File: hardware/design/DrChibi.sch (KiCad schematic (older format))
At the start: 20 parts, among them P1 PAD_SMD, P3 MultiPort, P4 IN+, P5 IN-, X1 MINI-USB-SHIELD-32005-201

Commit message: Six-phase power stage.
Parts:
- Rled3: renamed from R22; value 2k2 -> 100
- renumbered D2 to D1, D1 to D2, D4 to Dusb1, P3 to P1, P1 to P2, P4 to P3, P5 to P4, R14 to R1, R15 to R2, R38 to Rled1, R37 to Rled2, R6 to Rusb1, R103 to Rusb2, R104 to Rusb3
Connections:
- wire segments 74 -> 135
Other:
- moved on the sheet: Cbattfilt1, D1, D2, D3, Dusb1, P2, P3, P4, R1, R2, Rbatth1, Rbattl1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

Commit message: TODO: Routing of the DSBL-signals.
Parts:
- renumbered P1 to CONN1
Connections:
- wire segments 135 -> 142
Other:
- moved on the sheet: P3, P4
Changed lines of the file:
@@
 $Descr A4 11693 8268
 encoding utf-8
-Sheet 1 12
+Sheet 1 11
 Title "Long-Strip"
 Date "2016-02-15"
@@
 L CONN_1 P4
 U 1 1 53FA5B63
-P 9250 1350
-F 0 "P4" H 9330 1350 40  0000 L CNN
-F 1 "IN-" H 9250 1405 30  0001 C CNN
-F 2 "CRF1:1PAD_4x5mm" H 9250 1350 60  0001 C CNN
-F 3 "" H 9250 1350 60  0001 C CNN
-	1    9250 1350
+P 9250 2750
+F 0 "P4" H 9330 2750 40  0000 L CNN
+F 1 "IN-" H 9250 2805 30  0001 C CNN
+F 2 "CRF1:1PAD_4x5mm" H 9250 2750 60  0001 C CNN
+F 3 "" H 9250 2750 60  0001 C CNN
+	1    9250 2750
 	-1   0    0    1
 $EndComp
@@
 L CONN_1 P3
 U 1 1 53FA5B6A
-P 9250 1150
-F 0 "P3" H 9330 1150 40  0000 L CNN
-F 1 "IN+" H 9250 1205 30  0001 C CNN
-F 2 "CRF1:1PAD_4x5mm" H 9250 1150 60  0001 C CNN
-F 3 "" H 9250 1150 60  0001 C CNN
-	1    9250 1150
+P 9250 2550
+F 0 "P3" H 9330 2550 40  0000 L CNN
+F 1 "IN+" H 9250 2605 30  0001 C CNN
+F 2 "CRF1:1PAD_4x5mm" H 9250 2550 60  0001 C CNN
+F 3 "" H 9250 2550 60  0001 C CNN
+	1    9250 2550
 	-1   0    0    1
 $EndComp
@@
 DrChibi
 $Bitmap
-Pos 10700 3200
+Pos 10800 5000
 Scale 1,000000
 Data
@@
 	0    1    1    0
 $EndComp
-Text Notes 10050 1500 0    40   ~ 0
+Text Notes 10050 2900 0    40   ~ 0
 Voltage supply (5 - 24V)\nNeeds external decoupling\ncaps to avoid high voltage\ntransients produced by the\ninductance of the battery\nwiring while switching the FETs\nAlso critical for EMI/RF compliance
 $Comp
@@
 $EndSheet
 $Bitmap
-Pos 9700 5500
+Pos 9650 6250
 Scale 0,000000
 Data
@@
 EndData
 $EndBitmap
-Text Notes 9150 4900 0    60   ~ 0
+Text Notes 9100 5650 0    60   ~ 0
 Connect signal ground and\npower ground in one place only
 $Sheet
@@
 $EndComp
 $Sheet
-S 9650 2250 900  500
+S 9450 3350 900  500
 U 504F83BE
 F0 "Power Supply" 60
@@
 Connection ~ 2250 1100
 Wire Wire Line
-	9400 1450 9400 1350
-Wire Wire Line
-	10050 2700 10050 2700
+	9400 2850 9400 2750
 Wire Wire Line
 	2050 1900 1350 1900
@@
 	2550 2000 3150 2000
 Wire Notes Line
-	8950 900  10000 900
+	8950 2300 10000 2300
 Wire Notes Line
-	10000 950  10000 1650
+	10000 2350 10000 3050
 Wire Notes Line
-	10000 1650 8950 1650
+	10000 3050 8950 3050
 Wire Wire Line
 	2250 6000 2250 6000
@@
 	3150 2800 2750 2800
 $Sheet
-S 7550 750  800  400
+S 7900 750  800  900
 U 55DFCB16
 F0 "Virtual Y" 60
 F1 "virtual_y.sch" 60
-F2 "SENS1" I L 7550 800 60
-F3 "SENS2" I L 7550 900 60
-F4 "SENS3" I L 7550 1000 60
-F5 "SENSY" O L 7550 1100 60
+F2 "SENS1" I L 7900 800 60
+F3 "SENS2" I L 7900 900 60
+F4 "SENS3" I L 7900 1000 60
+F5 "SENSY1" O L 7900 1100 60
+F6 "SENS4" I L 7900 1250 60
+F7 "SENS5" I L 7900 1350 60
+F8 "SENS6" I L 7900 1450 60
+F9 "SENSY2" O L 7900 1600 60
 $EndSheet
 $Comp
-L GND #PWR11
+L GND #PWR01
 U 1 1 55E3ABA6
-P 9500 5150
-F 0 "#PWR11" H 9500 4900 50  0001 C CNN
-F 1 "GND" H 9500 5000 50  0000 C CNN
-F 2 "" H 9500 5150 60  0000 C CNN
-F 3 "" H 9500 5150 60  0000 C CNN
-	1    9500 5150
+P 9450 5900
+F 0 "#PWR01" H 9450 5650 50  0001 C CNN
+F 1 "GND" H 9450 5750 50  0000 C CNN
+F 2 "" H 9450 5900 60  0000 C CNN
+F 3 "" H 9450 5900 60  0000 C CNN
+	1    9450 5900
 	1    0    0    -1
 $EndComp
 $Comp
-L GNDPWR #PWR12
+L GNDPWR #PWR02
 U 1 1 55E3ADE6
-P 9800 5150
-F 0 "#PWR12" H 9800 4950 50  0001 C CNN
-F 1 "GNDPWR" H 9800 5020 50  0000 C CNN
-F 2 "" H 9800 5100 60  0000 C CNN
-F 3 "" H 9800 5100 60  0000 C CNN
-	1    9800 5150
+P 9750 5900
+F 0 "#PWR02" H 9750 5700 50  0001 C CNN
+F 1 "GNDPWR" H 9750 5770 50  0000 C CNN
+F 2 "" H 9750 5850 60  0000 C CNN
+F 3 "" H 9750 5850 60  0000 C CNN
+	1    9750 5900
 	1    0    0    -1
 $EndComp
 Wire Wire Line
-	9500 5150 9500 5050
+	9450 5900 9450 5800
 Wire Wire Line
-	9800 5050 9800 5150
+	9750 5800 9750 5900
 $Comp
-L GND #PWR5
+L GND #PWR03
 U 1 1 55E5268B
 P 2250 6400
-F 0 "#PWR5" H 2250 6150 50  0001 C CNN
+F 0 "#PWR03" H 2250 6150 50  0001 C CNN
 F 1 "GND" H 2250 6250 50  0000 C CNN
 F 2 "" H 2250 6400 60  0000 C CNN
@@
 $EndComp
 $Comp
-L GND #PWR6
+L GND #PWR04
 U 1 1 55E528C7
 P 2550 6400
-F 0 "#PWR6" H 2550 6150 50  0001 C CNN
+F 0 "#PWR04" H 2550 6150 50  0001 C CNN
 F 1 "GND" H 2550 6250 50  0000 C CNN
 F 2 "" H 2550 6400 60  0000 C CNN
@@
 $EndComp
 $Comp
-L GND #PWR8
+L GND #PWR05
 U 1 1 55E52B03
 P 2850 6400
-F 0 "#PWR8" H 2850 6150 50  0001 C CNN
+F 0 "#PWR05" H 2850 6150 50  0001 C CNN
 F 1 "GND" H 2850 6250 50  0000 C CNN
 F 2 "" H 2850 6400 60  0000 C CNN
@@
 $EndComp
 $Comp
-L GND #PWR4
+L GND #PWR06
 U 1 1 55E58E48
 P 1600 1350
-F 0 "#PWR4" H 1600 1100 50  0001 C CNN
+F 0 "#PWR06" H 1600 1100 50  0001 C CNN
 F 1 "GND" H 1600 1200 50  0000 C CNN
 F 2 "" H 1600 1350 60  0000 C CNN
@@
 $EndComp
 $Comp
-L GND #PWR2
+L GND #PWR07
 U 1 1 55E592AD
 P 1500 2300
-F 0 "#PWR2" H 1500 2050 50  0001 C CNN
+F 0 "#PWR07" H 1500 2050 50  0001 C CNN
 F 1 "GND" H 1500 2150 50  0000 C CNN
 F 2 "" H 1500 2300 60  0000 C CNN
@@
 $EndComp
 $Comp
-L GND #PWR1
+L GND #PWR08
 U 1 1 55E5EC55
 P 1150 3800
-F 0 "#PWR1" H 1150 3550 50  0001 C CNN
+F 0 "#PWR08" H 1150 3550 50  0001 C CNN
 F 1 "GND" H 1150 3650 50  0000 C CNN
 F 2 "" H 1150 3800 60  0000 C CNN
@@
 $EndComp
 $Comp
-L GNDPWR #PWR10
+L GNDPWR #PWR09
 U 1 1 55E81E9B
-P 9400 1450
-F 0 "#PWR10" H 9400 1250 50  0001 C CNN
-F 1 "GNDPWR" H 9400 1320 50  0000 C CNN
-F 2 "" H 9400 1400 60  0000 C CNN
-F 3 "" H 9400 1400 60  0000 C CNN
-	1    9400 1450
+P 9400 2850
+F 0 "#PWR09" H 9400 2650 50  0001 C CNN
+F 1 "GNDPWR" H 9400 2720 50  0000 C CNN
+F 2 "" H 9400 2800 60  0000 C CNN
+F 3 "" H 9400 2800 60  0000 C CNN
+	1    9400 2850
 	1    0    0    -1
 $EndComp
@@
 Goes to footprint
 $Comp
-L +24V #PWR9
+L +24V #PWR010
 U 1 1 56A6C8A8
-P 9400 1150
-F 0 "#PWR9" H 9400 1000 50  0001 C CNN
-F 1 "+24V" H 9418 1324 50  0000 C CNN
-F 2 "" H 9400 1150 50  0000 C CNN
-F 3 "" H 9400 1150 50  0000 C CNN
-	1    9400 1150
+P 9400 2550
+F 0 "#PWR010" H 9400 2400 50  0001 C CNN
+F 1 "+24V" H 9418 2724 50  0000 C CNN
+F 2 "" H 9400 2550 50  0000 C CNN
+F 3 "" H 9400 2550 50  0000 C CNN
+	1    9400 2550
 	1    0    0    -1
 $EndComp
 Wire Notes Line
-	8950 1600 8950 900
+	8950 3000 8950 2300
 $Comp
-L +24V #PWR3
+L +24V #PWR011
 U 1 1 56A9BA22
 P 1550 1000
-F 0 "#PWR3" H 1550 850 50  0001 C CNN
+F 0 "#PWR011" H 1550 850 50  0001 C CNN
 F 1 "+24V" H 1568 1174 50  0000 C CNN
 F 2 "" H 1550 1000 50  0000 C CNN
@@
 $EndComp
 $Comp
-L +5V #PWR7
+L +5V #PWR012
 U 1 1 56AA4E2C
 P 2800 1700
-F 0 "#PWR7" H 2800 1550 50  0001 C CNN
+F 0 "#PWR012" H 2800 1550 50  0001 C CNN
 F 1 "+5V" H 2818 1874 50  0000 C CNN
 F 2 "" H 2800 1700 50  0000 C CNN
@@
 	2250 5150 3150 5150
 $Comp
-L CONN_02X06 P1
+L CONN_02X06 CONN1
 U 1 1 56AF050D
 P 1100 4350
-F 0 "P1" H 1100 4908 50  0000 C CNN
+F 0 "CONN1" H 1100 4908 50  0000 C CNN
 F 1 "MultiPort" H 1100 4816 50  0000 C CNN
 F 2 "Socket_Strips:Socket_Strip_Straight_2x06" H 1100 4724 50  0000 C CNN
@@
 Connection ~ 5800 1300
 Wire Wire Line
-	7550 800  5800 800
+	5800 800  7900 800
 Wire Wire Line
 	5800 800  5800 1300
 Wire Wire Line
-	7550 900  7350 900
+	7350 900  7900 900
 Wire Wire Line
 	7350 900  7350 1750
@@
 Connection ~ 5800 2200
 Wire Wire Line
-	7550 1000 7400 1000
+	7400 1000 7900 1000
 Wire Wire Line
 	7400 1000 7400 2650
@@
 Connection ~ 5800 3100
 Wire Wire Line
-	7550 1100 7450 1100
+	7450 1100 7900 1100
 Wire Wire Line
 	5700 3550 7450 3550
@@
 	7450 3550 7450 1100
 $Sheet
-S 7550 3600 800  400
-U 56BBABF4
-F0 "Virtual Y2" 60
-F1 "virtual_y.sch" 60
-F2 "SENS1" I L 7550 3650 60
-F3 "SENS2" I L 7550 3750 60
-F4 "SENS3" I L 7550 3850 60
-F5 "SENSY" O L 7550 3950 60
-$EndSheet
-$Sheet
 S 6100 3750 1150 700
 U 56BC308A
@@
 Connection ~ 5800 4100
 Wire Wire Line
-	7550 3950 7450 3950
+	7450 3950 7700 3950
 Wire Wire Line
 	7450 3950 7450 6400
@@
 	7450 6400 5700 6400
 Wire Wire Line
-	7550 3850 7400 3850
+	7400 3850 7650 3850
 Wire Wire Line
 	7400 3850 7400 5450
@@
 Connection ~ 5800 5900
 Wire Wire Line
-	7550 3750 7350 3750
-Wire Wire Line
 	7350 3750 7350 4550
 Wire Wire Line
@@
 	5800 4550 5800 5000
 Connection ~ 5800 5000
+Wire Wire Line
+	7550 3650 7550 1250
+Wire Wire Line
+	7550 1250 7900 1250
+Wire Wire Line
+	7600 1350 7900 1350
+Wire Wire Line
+	7600 1350 7600 3750
+Wire Wire Line
+	7600 3750 7350 3750
+Wire Wire Line
+	7650 3850 7650 1450
+Wire Wire Line
+	7650 1450 7900 1450
+Wire Wire Line
+	7700 3950 7700 1600
+Wire Wire Line
+	7700 1600 7900 1600
 $EndSCHEMATC

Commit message: TODO: Find appropriate routing to CPU
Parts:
- Rbatth1, Rbattl1: footprint Resistors_SMD:R_0603_HandSoldering -> Resistors_SMD:R_0603
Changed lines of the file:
@@
 F 0 "Rbatth1" V 1550 1000 50  0000 C CNN
 F 1 "10k" V 1642 1000 50  0000 C CNN
-F 2 "Resistors_SMD:R_0603_HandSoldering" V 1734 1000 50  0000 C CNN
+F 2 "Resistors_SMD:R_0603" V 1734 1000 50  0000 C CNN
 F 3 "" H 1850 1000 50  0000 C CNN
 	1    1850 1000
@@
 F 0 "Rbattl1" V 1550 1100 50  0000 C CNN
 F 1 "1k5" V 1642 1100 50  0000 C CNN
-F 2 "Resistors_SMD:R_0603_HandSoldering" V 1734 1100 50  0000 C CNN
+F 2 "Resistors_SMD:R_0603" V 1734 1100 50  0000 C CNN
 F 3 "" H 1850 1100 50  0000 C CNN
 	1    1850 1100

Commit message: TODO next: Rearrangement and routing of the analog inputs.
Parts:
- CONN1: footprint Socket_Strips:Socket_Strip_Straight_2x06 -> Pads:Pin_Header_Straight_2x06_Pitch1.27mm
- X1: footprint CRF1:con-cypressindustries-32005-201 -> Pads:MICRO-B_USB
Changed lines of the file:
@@
 F 0 "X1" H 1428 2046 50  0000 L CNN
 F 1 "MINI-USB-SHIELD-32005-201" H 1428 1954 50  0000 L CNN
-F 2 "CRF1:con-cypressindustries-32005-201" H 1150 2150 50  0001 C CNN
+F 2 "Pads:MICRO-B_USB" H 1150 2150 50  0001 C CNN
 F 3 "" H 1150 2000 60  0001 C CNN
 	1    1150 2000
@@
 F 0 "CONN1" H 1100 4908 50  0000 C CNN
 F 1 "MultiPort" H 1100 4816 50  0000 C CNN
-F 2 "Socket_Strips:Socket_Strip_Straight_2x06" H 1100 4724 50  0000 C CNN
+F 2 "Pads:Pin_Header_Straight_2x06_Pitch1.27mm" H 1100 4724 50  0000 C CNN
 F 3 "" H 1100 3150 50  0000 C CNN
 	1    1100 4350

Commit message: Some more routing...
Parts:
- removed CONN1: MultiPort, Pads:Pin_Header_Straight_2x06_Pitch1.27mm, symbol CONN_02X06
- added P1: CONN_02X05, Pads:Pin_Header_Straight_2x05_Pitch1.27mm, symbol CONN_02X05
- added PCANGND1: PAD_SMD, Pads:PAD_SMD_3x3, symbol PAD_SMD
- added PCANH1, PCANL1, PCANVCC1: PAD_SMD, Pads:PAD_SMD_1.2x2.5, symbol PAD_SMD
- P3: footprint CRF1:1PAD_4x5mm -> Pads:1PAD_3x6mm
- P4: footprint CRF1:1PAD_4x5mm -> Pads:1PAD_3.5x6mm
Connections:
- wire segments 142 -> 147
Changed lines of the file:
@@
 F 0 "P4" H 9330 2750 40  0000 L CNN
 F 1 "IN-" H 9250 2805 30  0001 C CNN
-F 2 "CRF1:1PAD_4x5mm" H 9250 2750 60  0001 C CNN
+F 2 "Pads:1PAD_3.5x6mm" H 9250 2750 60  0001 C CNN
 F 3 "" H 9250 2750 60  0001 C CNN
 	1    9250 2750
@@
 F 0 "P3" H 9330 2550 40  0000 L CNN
 F 1 "IN+" H 9250 2605 30  0001 C CNN
-F 2 "CRF1:1PAD_4x5mm" H 9250 2550 60  0001 C CNN
+F 2 "Pads:1PAD_3x6mm" H 9250 2550 60  0001 C CNN
 F 3 "" H 9250 2550 60  0001 C CNN
 	1    9250 2550
@@
 F4 "CANH" I L 1900 2700 60
 F5 "CANL" I L 1900 2800 60
+F6 "VCC2" I L 1900 2600 60
+F7 "GND2" I L 1900 2900 60
 $EndSheet
 $Comp
@@
 20 08 82 20 08 12 3C 28 79 08 82 20 08 82 20 2D 08 4A 1E 82 20 08 82 20 48 0B 82 92 87 20 08 82
 20 08 D2 82 A0 E4 21 08 82 20 08 82 B4 20 28 79 08 82 20 08 82 20 2D 08 4A 1E 82 20 08 82 20 48
-0B F2 FF 19 12 7F 86 40 CA 02 9D 00 00 00 00 49 45 4E 44 AE 42 60 82 FF
+0B F2 FF 19 12 7F 86 40 CA 02 9D 00 00 00 00 49 45 4E 44 AE 42 60 82 00
 EndData
 $EndBitmap
@@
 L GND #PWR08
 U 1 1 55E5EC55
-P 1150 3800
-F 0 "#PWR08" H 1150 3550 50  0001 C CNN
-F 1 "GND" H 1150 3650 50  0000 C CNN
-F 2 "" H 1150 3800 60  0000 C CNN
-F 3 "" H 1150 3800 60  0000 C CNN
-	1    1150 3800
-	0    -1   -1   0
+P 850 4200
+F 0 "#PWR08" H 850 3950 50  0001 C CNN
+F 1 "GND" H 850 4050 50  0000 C CNN
+F 2 "" H 850 4200 60  0000 C CNN
+F 3 "" H 850 4200 60  0000 C CNN
+	1    850  4200
+	0    1    1    0
 $EndComp
 $Comp
@@
 Wire Wire Line
 	2250 5150 3150 5150
-$Comp
-L CONN_02X06 CONN1
-U 1 1 56AF050D
-P 1100 4350
-F 0 "CONN1" H 1100 4908 50  0000 C CNN
-F 1 "MultiPort" H 1100 4816 50  0000 C CNN
-F 2 "Pads:Pin_Header_Straight_2x06_Pitch1.27mm" H 1100 4724 50  0000 C CNN
-F 3 "" H 1100 3150 50  0000 C CNN
-	1    1100 4350
-	1    0    0    -1
-$EndComp
-Wire Wire Line
-	3150 3650 800  3650
-Wire Wire Line
-	800  3650 800  4200
-Wire Wire Line
-	800  4200 850  4200
-Wire Wire Line
-	3150 3550 750  3550
-Wire Wire Line
-	750  3550 750  4300
-Wire Wire Line
-	750  4300 850  4300
-Wire Wire Line
-	3150 3450 700  3450
-Wire Wire Line
-	700  3450 700  4400
-Wire Wire Line
-	700  4400 850  4400
-Wire Wire Line
-	1900 2800 650  2800
 Wire Wire Line
-	650  2800 650  4500
+	600  3650 3150 3650
 Wire Wire Line
-	650  4500 850  4500
+	550  3550 3150 3550
 Wire Wire Line
-	1900 2700 600  2700
+	500  3450 3150 3450
 Wire Wire Line
-	600  2700 600  4600
-Wire Wire Line
-	600  4600 850  4600
-Wire Wire Line
-	1150 3800 850  3800
-Wire Wire Line
-	850  3800 850  4100
-Wire Wire Line
-	3150 3850 1350 3850
-Wire Wire Line
-	1350 3850 1350 4100
+	650  3850 3150 3850
 Wire Wire Line
 	1350 4500 3150 4500
@@
 Wire Wire Line
 	7700 1600 7900 1600
+$Comp
+L PAD_SMD PCANVCC1
+U 1 1 56DB50A7
+P 1100 2550
+F 0 "PCANVCC1" H 1228 2656 60  0000 L CNN
+F 1 "PAD_SMD" H 1228 2550 60  0000 L CNN
+F 2 "Pads:PAD_SMD_1.2x2.5" H 1228 2444 60  0000 L CNN
+F 3 "" H 1100 2400 60  0000 C CNN
+	1    1100 2550
+	-1   0    0    -1
+$EndComp
+$Comp
+L PAD_SMD PCANH1
+U 1 1 56DB5C72
+P 1100 2800
+F 0 "PCANH1" H 1228 2906 60  0000 L CNN
+F 1 "PAD_SMD" H 1228 2800 60  0000 L CNN
+F 2 "Pads:PAD_SMD_1.2x2.5" H 1228 2694 60  0000 L CNN
+F 3 "" H 1100 2650 60  0000 C CNN
+	1    1100 2800
+	-1   0    0    -1
+$EndComp
+$Comp
+L PAD_SMD PCANL1
+U 1 1 56DB6368
+P 1100 3050
+F 0 "PCANL1" H 1228 3156 60  0000 L CNN
+F 1 "PAD_SMD" H 1228 3050 60  0000 L CNN
+F 2 "Pads:PAD_SMD_1.2x2.5" H 1228 2944 60  0000 L CNN
+F 3 "" H 1100 2900 60  0000 C CNN
+	1    1100 3050
+	-1   0    0    -1
+$EndComp
+$Comp
+L PAD_SMD PCANGND1
+U 1 1 56DB6A40
+P 1100 3300
+F 0 "PCANGND1" H 1228 3406 60  0000 L CNN
+F 1 "PAD_SMD" H 1228 3300 60  0000 L CNN
+F 2 "Pads:PAD_SMD_3x3" H 1228 3194 60  0000 L CNN
+F 3 "" H 1100 3150 60  0000 C CNN
+	1    1100 3300
+	-1   0    0    -1
+$EndComp
+Wire Wire Line
+	1300 2550 1550 2550
+Wire Wire Line
+	1550 2550 1550 2600
+Wire Wire Line
+	1550 2600 1900 2600
+Wire Wire Line
+	1300 2800 1350 2800
+Wire Wire Line
+	1350 2800 1350 2700
+Wire Wire Line
+	1350 2700 1900 2700
+Wire Wire Line
+	1300 3050 1450 3050
+Wire Wire Line
+	1450 3050 1450 2800
+Wire Wire Line
+	1450 2800 1900 2800
+Wire Wire Line
+	1300 3300 1550 3300
+Wire Wire Line
+	1550 3300 1550 2900
+Wire Wire Line
+	1550 2900 1900 2900
+$Comp
+L CONN_02X05 P1
+U 1 1 56DBBF3B
+P 1100 4400
+F 0 "P1" H 1100 4908 50  0000 C CNN
+F 1 "CONN_02X05" H 1100 4816 50  0000 C CNN
+F 2 "Pads:Pin_Header_Straight_2x05_Pitch1.27mm" H 1100 4724 50  0000 C CNN
+F 3 "" H 1100 3200 50  0000 C CNN
+	1    1100 4400
+	1    0    0    -1
+$EndComp
+Wire Wire Line
+	650  3850 650  4300
+Wire Wire Line
+	650  4300 850  4300
+Wire Wire Line
+	600  3650 600  4400
+Wire Wire Line
+	600  4400 850  4400
+Wire Wire Line
+	550  3550 550  4500
+Wire Wire Line
+	550  4500 850  4500
+Wire Wire Line
+	500  3450 500  4600
+Wire Wire Line
+	500  4600 850  4600
 $EndSCHEMATC

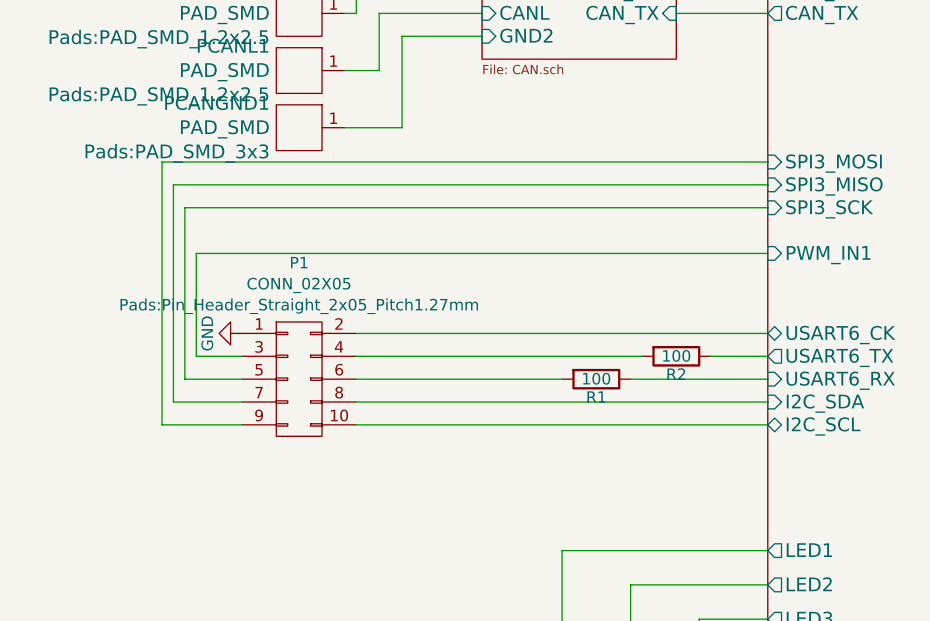
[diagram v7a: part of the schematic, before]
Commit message: Changed pin for LED3
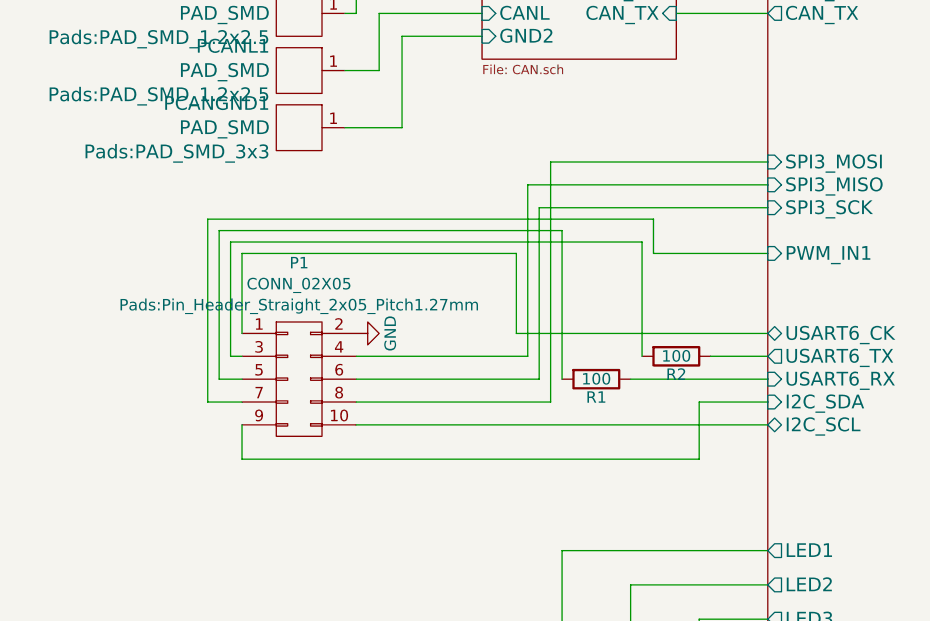
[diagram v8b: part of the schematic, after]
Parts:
- Rled3: footprint Resistors_SMD:R_0603_HandSoldering -> Resistors_SMD:R_0603
- Rusb1, Rusb2, Rusb3: footprint Resistors_SMD:R_0603 -> Resistors_SMD:R_0402
- X1: footprint Pads:MICRO-B_USB -> CRF1:mini_USB_gnd
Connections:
- net GND: now also P1.2 (P2); no longer P1.1 (P1)
- net MCU/I2C_SDA: now also P1.9 (P9); no longer P1.8 (P8)
- net MCU/PWM_IN1: now also P1.7 (P7); no longer P1.3 (P3)
- net MCU/SPI3_MISO: now also P1.4 (P4); no longer P1.7 (P7)
- net MCU/SPI3_MOSI: now also P1.8 (P8); no longer P1.9 (P9)
- net MCU/SPI3_SCK: now also P1.6 (P6); no longer P1.5 (P5)
- net MCU/USART6_CK: now also P1.1 (P1); no longer P1.2 (P2)
- net at R2.2: now also P1.3 (P3); no longer P1.4 (P4)
- net at R1.2: now also P1.5 (P5); no longer P1.6 (P6)
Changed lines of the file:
@@
 F 0 "X1" H 1428 2046 50  0000 L CNN
 F 1 "MINI-USB-SHIELD-32005-201" H 1428 1954 50  0000 L CNN
-F 2 "Pads:MICRO-B_USB" H 1150 2150 50  0001 C CNN
+F 2 "CRF1:mini_USB_gnd" H 1150 2150 50  0001 C CNN
 F 3 "" H 1150 2000 60  0001 C CNN
 	1    1150 2000
@@
 F 0 "Rusb2" V 2112 1900 40  0000 C CNN
 F 1 "22R" V 2190 1900 40  0000 C CNN
-F 2 "Resistors_SMD:R_0603" V 2230 1900 30  0001 C CNN
+F 2 "Resistors_SMD:R_0402" V 2230 1900 30  0001 C CNN
 F 3 "" H 2300 1900 30  0000 C CNN
 	1    2300 1900
@@
 F 0 "Rusb3" V 2112 2000 40  0000 C CNN
 F 1 "22R" V 2190 2000 40  0000 C CNN
-F 2 "Resistors_SMD:R_0603" V 2230 2000 30  0001 C CNN
+F 2 "Resistors_SMD:R_0402" V 2230 2000 30  0001 C CNN
 F 3 "" H 2300 2000 30  0000 C CNN
 	1    2300 2000
@@
 F 0 "Rled3" V 2750 5750 50  0000 C CNN
 F 1 "100" V 2850 5750 50  0000 C CNN
-F 2 "Resistors_SMD:R_0603_HandSoldering" H 2850 5750 60  0001 C CNN
+F 2 "Resistors_SMD:R_0603" H 2850 5750 60  0001 C CNN
 F 3 "" H 2850 5750 60  0001 C CNN
 	1    2850 5750
@@
 F 0 "Rusb1" V 1830 2200 50  0000 C CNN
 F 1 "10k" V 1750 2200 50  0000 C CNN
-F 2 "Resistors_SMD:R_0603" V 1680 2200 30  0001 C CNN
+F 2 "Resistors_SMD:R_0402" V 1680 2200 30  0001 C CNN
 F 3 "" H 1750 2200 30  0000 C CNN
 	1    1750 2200
@@
 	2550 4400 3150 4400
 Wire Wire Line
-	2600 4300 1350 4300
-Wire Wire Line
-	2250 4400 1350 4400
-Wire Wire Line
 	1350 1800 2100 1800
 Wire Wire Line
@@
 L GND #PWR08
 U 1 1 55E5EC55
-P 850 4200
-F 0 "#PWR08" H 850 3950 50  0001 C CNN
-F 1 "GND" H 850 4050 50  0000 C CNN
-F 2 "" H 850 4200 60  0000 C CNN
-F 3 "" H 850 4200 60  0000 C CNN
-	1    850  4200
-	0    1    1    0
+P 1350 4200
+F 0 "#PWR08" H 1350 3950 50  0001 C CNN
+F 1 "GND" H 1350 4050 50  0000 C CNN
+F 2 "" H 1350 4200 60  0000 C CNN
+F 3 "" H 1350 4200 60  0000 C CNN
+	1    1350 4200
+	0    -1   -1   0
 $EndComp
 $Comp
@@
 Wire Wire Line
 	5900 1600 6100 1600
-Wire Wire Line
-	1350 4200 3150 4200
 $Comp
 L R Rbatth1
@@
 Wire Wire Line
 	2250 5150 3150 5150
-Wire Wire Line
-	600  3650 3150 3650
-Wire Wire Line
-	550  3550 3150 3550
-Wire Wire Line
-	500  3450 3150 3450
-Wire Wire Line
-	650  3850 3150 3850
-Wire Wire Line
-	1350 4500 3150 4500
-Wire Wire Line
-	1350 4600 3150 4600
 Connection ~ 5950 1500
 Connection ~ 5900 1600
@@
 $EndComp
 Wire Wire Line
-	650  3850 650  4300
+	3150 4200 2050 4200
+Wire Wire Line
+	2050 4200 2050 3850
+Wire Wire Line
+	2050 3850 850  3850
+Wire Wire Line
+	850  3850 850  4200
+Wire Wire Line
+	2600 4300 2600 3800
+Wire Wire Line
+	2600 3800 800  3800
+Wire Wire Line
+	800  3800 800  4300
+Wire Wire Line
+	800  4300 850  4300
+Wire Wire Line
+	2250 4400 2250 3750
+Wire Wire Line
+	2250 3750 750  3750
+Wire Wire Line
+	750  3750 750  4400
+Wire Wire Line
+	750  4400 850  4400
+Wire Wire Line
+	3150 3850 2650 3850
+Wire Wire Line
+	2650 3850 2650 3700
+Wire Wire Line
+	2650 3700 700  3700
+Wire Wire Line
+	700  3700 700  4500
+Wire Wire Line
+	700  4500 850  4500
+Wire Wire Line
+	3150 3550 2100 3550
+Wire Wire Line
+	2100 3550 2100 4300
+Wire Wire Line
+	2100 4300 1350 4300
+Wire Wire Line
+	1350 4600 3150 4600
+Wire Wire Line
+	850  4750 850  4600
+Wire Wire Line
+	3150 3650 2150 3650
+Wire Wire Line
+	2150 3650 2150 4400
 Wire Wire Line
-	650  4300 850  4300
+	2150 4400 1350 4400
 Wire Wire Line
-	600  3650 600  4400
+	3150 3450 2200 3450
 Wire Wire Line
-	600  4400 850  4400
+	2200 3450 2200 4500
 Wire Wire Line
-	550  3550 550  4500
+	2200 4500 1350 4500
 Wire Wire Line
-	550  4500 850  4500
+	3150 4500 2850 4500
 Wire Wire Line
-	500  3450 500  4600
+	2850 4500 2850 4750
 Wire Wire Line
-	500  4600 850  4600
+	2850 4750 850  4750
 $EndSCHEMATC
